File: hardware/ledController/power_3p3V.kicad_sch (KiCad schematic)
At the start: 11 parts, among them U1 ISL85415

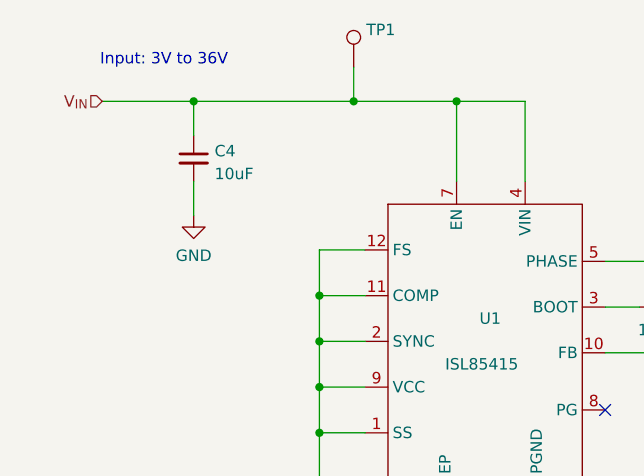
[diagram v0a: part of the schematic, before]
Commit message: First attempt of schematic to PCB
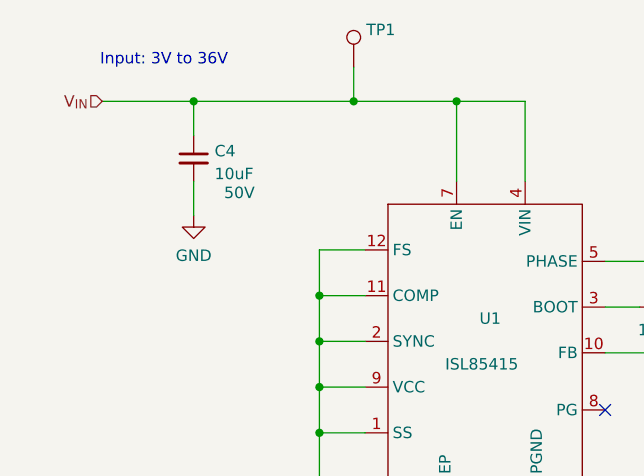
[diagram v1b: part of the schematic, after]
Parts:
- C4: footprint (none) -> Capacitor_SMD:C_1206_3216Metric_Pad1.33x1.80mm_HandSolder; Voltage (none) -> 50V
- C5, C6, C7, C8: footprint (none) -> Capacitor_SMD:C_0402_1005Metric_Pad0.74x0.62mm_HandSolder
- R1, R2: footprint (none) -> Resistor_SMD:R_0603_1608Metric_Pad0.98x0.95mm_HandSolder
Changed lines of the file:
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@@
     (property "Reference" "C6" (id 0) (at 158.75 83.82 90))
     (property "Value" "100nF" (id 1) (at 158.75 88.9 90))
-    (property "Footprint" "" (id 2) (at 158.75 86.36 0)
+    (property "Footprint" "Capacitor_SMD:C_0402_1005Metric_Pad0.74x0.62mm_HandSolder" (id 2) (at 158.75 86.36 0)
       (effects (font (size 1.27 1.27)) hide)
     )
@@
       (effects (font (size 1.27 1.27)) (justify left))
     )
-    (property "Footprint" "" (id 2) (at 176.53 86.36 0)
+    (property "Footprint" "Resistor_SMD:R_0603_1608Metric_Pad0.98x0.95mm_HandSolder" (id 2) (at 176.53 86.36 0)
       (effects (font (size 1.27 1.27)) hide)
     )
@@
   )
   (symbol (lib_id "Device:C_Small") (at 106.68 69.85 0) (unit 1)
-    (in_bom yes) (on_board yes) (fields_autoplaced)
+    (in_bom yes) (on_board yes)
     (property "Reference" "C4" (id 0) (at 109.0041 69.0216 0)
       (effects (font (size 1.27 1.27)) (justify left))
@@
       (effects (font (size 1.27 1.27)) (justify left))
     )
-    (property "Footprint" "" (id 2) (at 106.68 69.85 0)
+    (property "Footprint" "Capacitor_SMD:C_1206_3216Metric_Pad1.33x1.80mm_HandSolder" (id 2) (at 106.68 69.85 0)
       (effects (font (size 1.27 1.27)) hide)
     )
@@
       (effects (font (size 1.27 1.27)) hide)
     )
+    (property "Voltage" "50V" (id 4) (at 111.76 73.66 0))
     (pin "1")
     (pin "2")
@@
       (effects (font (size 1.27 1.27)) (justify left))
     )
-    (property "Footprint" "" (id 2) (at 200.66 87.63 0)
+    (property "Footprint" "Capacitor_SMD:C_0402_1005Metric_Pad0.74x0.62mm_HandSolder" (id 2) (at 200.66 87.63 0)
       (effects (font (size 1.27 1.27)) hide)
     )
@@
       (effects (font (size 1.27 1.27)) (justify left))
     )
-    (property "Footprint" "" (id 2) (at 187.96 87.63 0)
+    (property "Footprint" "Capacitor_SMD:C_0402_1005Metric_Pad0.74x0.62mm_HandSolder" (id 2) (at 187.96 87.63 0)
       (effects (font (size 1.27 1.27)) hide)
     )
@@
       (effects (font (size 1.27 1.27)) (justify left))
     )
-    (property "Footprint" "" (id 2) (at 176.53 97.79 0)
+    (property "Footprint" "Resistor_SMD:R_0603_1608Metric_Pad0.98x0.95mm_HandSolder" (id 2) (at 176.53 97.79 0)
       (effects (font (size 1.27 1.27)) hide)
     )
@@
       (effects (font (size 1.27 1.27)) (justify left))
     )
-    (property "Footprint" "" (id 2) (at 120.65 107.95 0)
-      (effects (font (size 1.27 1.27)) hide)
-    )
+    (property "Footprint" "Capacitor_SMD:C_0402_1005Metric_Pad0.74x0.62mm_HandSolder" (id 2) (at 120.65 107.95 0)
+      (effects (font (size 1.27 1.27)) hide)
+    )
